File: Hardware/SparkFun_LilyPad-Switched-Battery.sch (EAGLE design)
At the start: 11 parts

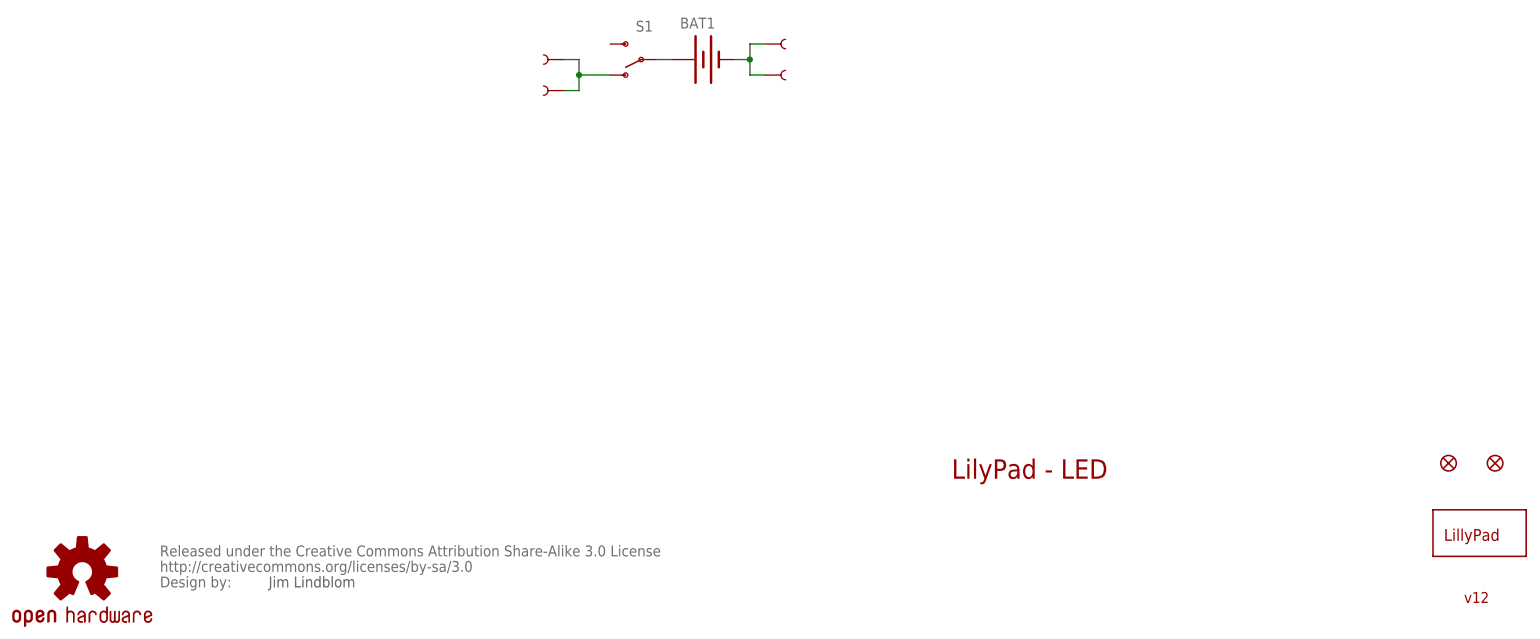
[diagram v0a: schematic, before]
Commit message: Add board thickness
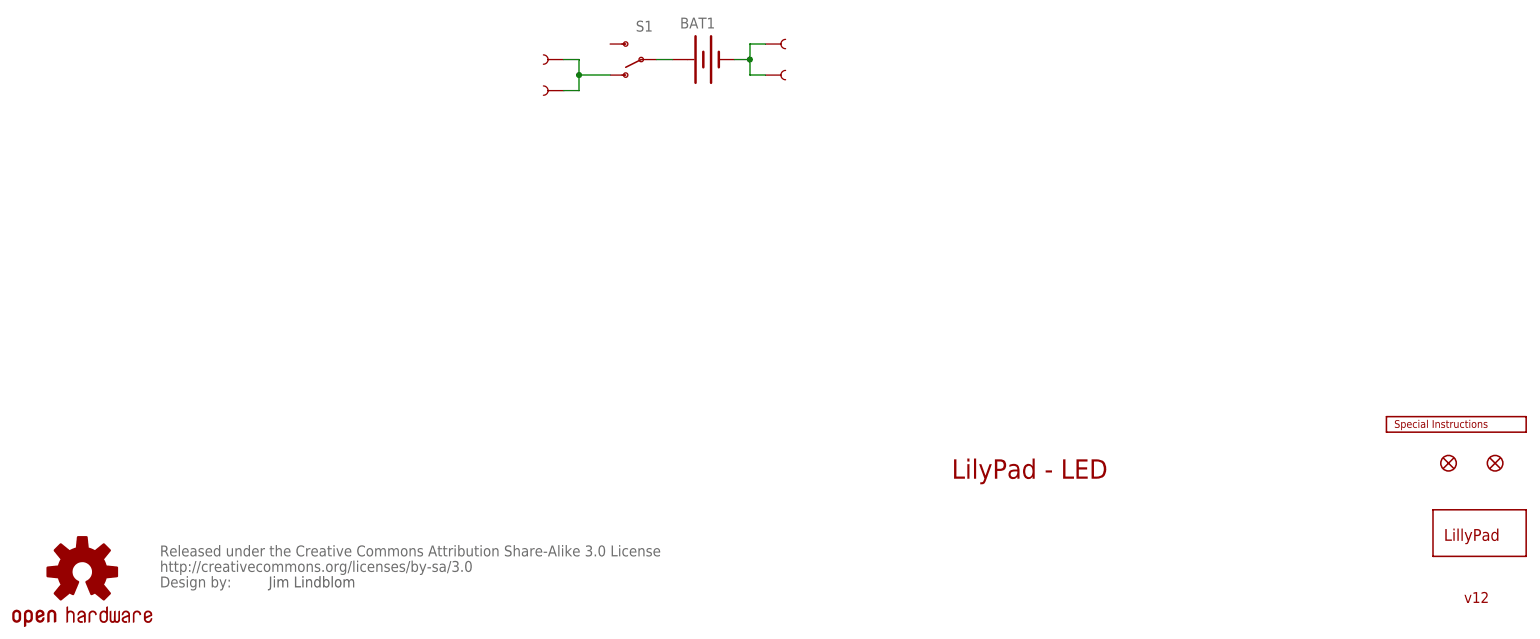
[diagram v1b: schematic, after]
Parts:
- added LOGO1: SPECIAL_INSTRUCTIONS-ORDERING, SparkFun-Aesthetics:SPECIAL_INSTRUCTIONS-ORDERING
